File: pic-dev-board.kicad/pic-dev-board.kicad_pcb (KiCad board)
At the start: 2 copper layers, 100 x 100 mm, 74 parts, among them J1 Conn_GP0, J10 Jumper DATin, J11 Conn_SR_2, J12 Conn_SR_1, J13 Conn_5V_GND, J14 Jumper CLKin, J15 Barrel_Jack_Switch, J16 RUN/~PGM, J17 I2C, J18 GP1(RA1)/RB6, J19 GP2(RA2)/RB4, J2 Conn_GP4, J3 Conn_GP1, J4 Conn_GP5, J5 Conn_GP2, J6 Conn_ICSP, J7 Conn_TRISC, J8 Conn_TRISA, J9 Conn_TRISB, SW1 SW_Push, U1 PIC16F690-IP, U2 74HC595, U3 74HC595

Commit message: added second GP/TRISA connector
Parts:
- added J20: Conn_TRISA, Connector_PinHeader_2.54mm:PinHeader_1x07_P2.54mm_Vertical, F.Cu at (44.6, 104.0)
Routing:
- net /GP0: track 139.8 -> 222.0 mm
- net /GP1: track 114.7 -> 196.4 mm
- net /GP5: track 114.7 -> 196.4 mm
- net /GP4: track 112.4 -> 194.0 mm
- net /GP2: track 115.7 -> 197.4 mm
- net +5V: track 356.6 -> 389.5 mm
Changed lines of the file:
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@@
     (thickness 1.6)
     (drawings 8)
-    (tracks 648)
+    (tracks 672)
     (zones 0)
-    (modules 74)
+    (modules 75)
     (nets 88)
   )
@@
     (add_net /Vdd)
   )
+  (module Connector_PinHeader_2.54mm:PinHeader_1x07_P2.54mm_Vertical (layer F.Cu)
+    (at 44.6278 104.013)
+    (descr "Through hole straight pin header, 1x07, 2.54mm pitch, single row")
+    (tags "Through hole pin header THT 1x07 2.54mm single row")
+    (fp_text reference J20 (at 0 -2.33) (layer F.SilkS) hide
+      (effects (font (size 1 1) (thickness 0.15)))
+    )
+    (fp_text value Conn_TRISA (at 0 17.57) (layer F.Fab)
+      (effects (font (size 1 1) (thickness 0.15)))
+    )
+    (fp_text user %R (at 0 7.62 90) (layer F.Fab)
+      (effects (font (size 1 1) (thickness 0.15)))
+    )
+    (fp_line (start 1.8 -1.8) (end -1.8 -1.8) (layer F.CrtYd) (width 0.05))
+    (fp_line (start 1.8 17.05) (end 1.8 -1.8) (layer F.CrtYd) (width 0.05))
+    (fp_line (start -1.8 17.05) (end 1.8 17.05) (layer F.CrtYd) (width 0.05))
+    (fp_line (start -1.8 -1.8) (end -1.8 17.05) (layer F.CrtYd) (width 0.05))
+    (fp_line (start -1.33 -1.33) (end 0 -1.33) (layer F.SilkS) (width 0.12))
+    (fp_line (start -1.33 0) (end -1.33 -1.33) (layer F.SilkS) (width 0.12))
+    (fp_line (start -1.33 1.27) (end 1.33 1.27) (layer F.SilkS) (width 0.12))
+    (fp_line (start 1.33 1.27) (end 1.33 16.57) (layer F.SilkS) (width 0.12))
+    (fp_line (start -1.33 1.27) (end -1.33 16.57) (layer F.SilkS) (width 0.12))
+    (fp_line (start -1.33 16.57) (end 1.33 16.57) (layer F.SilkS) (width 0.12))
+    (fp_line (start -1.27 -0.635) (end -0.635 -1.27) (layer F.Fab) (width 0.1))
+    (fp_line (start -1.27 16.51) (end -1.27 -0.635) (layer F.Fab) (width 0.1))
+    (fp_line (start 1.27 16.51) (end -1.27 16.51) (layer F.Fab) (width 0.1))
+    (fp_line (start 1.27 -1.27) (end 1.27 16.51) (layer F.Fab) (width 0.1))
+    (fp_line (start -0.635 -1.27) (end 1.27 -1.27) (layer F.Fab) (width 0.1))
+    (pad 7 thru_hole oval (at 0 15.24) (size 1.7 1.7) (drill 1) (layers *.Cu *.Mask)
+      (net 53 +5V))
+    (pad 6 thru_hole oval (at 0 12.7) (size 1.7 1.7) (drill 1) (layers *.Cu *.Mask)
+      (net 2 GND))
+    (pad 5 thru_hole oval (at 0 10.16) (size 1.7 1.7) (drill 1) (layers *.Cu *.Mask)
+      (net 59 /GP5))
+    (pad 4 thru_hole oval (at 0 7.62) (size 1.7 1.7) (drill 1) (layers *.Cu *.Mask)
+      (net 55 /GP4))
+    (pad 3 thru_hole oval (at 0 5.08) (size 1.7 1.7) (drill 1) (layers *.Cu *.Mask)
+      (net 61 /GP2))
+    (pad 2 thru_hole oval (at 0 2.54) (size 1.7 1.7) (drill 1) (layers *.Cu *.Mask)
+      (net 57 /GP1))
+    (pad 1 thru_hole rect (at 0 0) (size 1.7 1.7) (drill 1) (layers *.Cu *.Mask)
+      (net 51 /GP0))
+    (model ${KISYS3DMOD}/Connector_PinHeader_2.54mm.3dshapes/PinHeader_1x07_P2.54mm_Vertical.wrl
+      (at (xyz 0 0 0))
+      (scale (xyz 1 1 1))
+      (rotate (xyz 0 0 0))
+    )
+  )
   (module user:PinHeader_2x15_P2.54mm_Vertical_Slim (layer F.Cu)
     (at 80.772 91.186)
@@
   (segment (start 122.174 89.962136) (end 122.174 101.938) (width 0.25) (layer F.Cu) (net 51))
   (segment (start 122.174 101.938) (end 124.122 103.886) (width 0.25) (layer F.Cu) (net 51))
+  (segment (start 44.6278 102.913) (end 44.6278 104.013) (width 0.25) (layer B.Cu) (net 51))
+  (segment (start 44.829801 102.710999) (end 44.6278 102.913) (width 0.25) (layer B.Cu) (net 51))
+  (segment (start 116.896001 102.710999) (end 44.829801 102.710999) (width 0.25) (layer B.Cu) (net 51))
+  (segment (start 118.071002 103.886) (end 116.896001 102.710999) (width 0.25) (layer B.Cu) (net 51))
+  (segment (start 125.222 103.886) (end 118.071002 103.886) (width 0.25) (layer B.Cu) (net 51))
   (segment (start 120.045389 31.602589) (end 53.055011 31.602589) (width 0.25) (layer F.Cu) (net 52))
   (segment (start 52.08 32.5776) (end 52.08 34.1276) (width 0.25) (layer F.Cu) (net 52))
@@
   (segment (start 47.4946 89.408) (end 71.12 89.408) (width 0.5) (layer F.Cu) (net 53))
   (segment (start 45.5896 87.503) (end 47.4946 89.408) (width 0.5) (layer F.Cu) (net 53))
-  (segment (start 43.7896 87.503) (end 45.5896 87.503) (width 0.5) (layer F.Cu) (net 53))
   (segment (start 43.7896 87.503) (end 43.7896 74.2442) (width 0.5) (layer B.Cu) (net 53))
   (segment (start 37.3126 67.7672) (end 33.274 67.7672) (width 0.5) (layer B.Cu) (net 53))
@@
   (segment (start 43.434 61.7991) (end 41.944098 61.7991) (width 0.5) (layer F.Cu) (net 53))
   (segment (start 43.434 61.7991) (end 46.4566 61.7991) (width 0.5) (layer F.Cu) (net 53))
+  (segment (start 46.451999 88.365399) (end 45.5896 87.503) (width 0.5) (layer F.Cu) (net 53))
+  (segment (start 46.451999 117.428801) (end 46.451999 88.365399) (width 0.5) (layer F.Cu) (net 53))
+  (segment (start 45.5896 87.503) (end 43.7896 87.503) (width 0.5) (layer F.Cu) (net 53))
+  (segment (start 44.6278 119.253) (end 46.451999 117.428801) (width 0.5) (layer F.Cu) (net 53))
   (segment (start 98.468 71.374) (end 96.4955 71.374) (width 0.25) (layer F.Cu) (net 54))
   (segment (start 99.568 71.374) (end 98.468 71.374) (width 0.25) (layer F.Cu) (net 54))
@@
   (segment (start 101.9048 82.804) (end 103.244399 84.143599) (width 0.25) (layer F.Cu) (net 55))
   (segment (start 104.807001 106.800003) (end 104.807001 88.957401) (width 0.25) (layer F.Cu) (net 55))
+  (segment (start 45.477799 110.783001) (end 44.6278 111.633) (width 0.25) (layer B.Cu) (net 55))
+  (segment (start 45.929801 110.330999) (end 45.477799 110.783001) (width 0.25) (layer B.Cu) (net 55))
+  (segment (start 124.046999 110.330999) (end 45.929801 110.330999) (width 0.25) (layer B.Cu) (net 55))
+  (segment (start 125.222 111.506) (end 124.046999 110.330999) (width 0.25) (layer B.Cu) (net 55))
   (segment (start 99.568 82.804) (end 96.4955 82.804) (width 0.25) (layer F.Cu) (net 56))
   (segment (start 50.546 48.514) (end 50.546 49.711002) (width 0.25) (layer F.Cu) (net 57))
@@
   (segment (start 115.64049 88.755488) (end 120.396 93.510998) (width 0.25) (layer F.Cu) (net 57))
   (segment (start 109.53249 83.113626) (end 109.53249 83.639354) (width 0.25) (layer F.Cu) (net 57))
+  (segment (start 45.477799 105.703001) (end 44.6278 106.553) (width 0.25) (layer B.Cu) (net 57))
+  (segment (start 46.119799 105.061001) (end 45.477799 105.703001) (width 0.25) (layer B.Cu) (net 57))
+  (segment (start 123.857001 105.061001) (end 46.119799 105.061001) (width 0.25) (layer B.Cu) (net 57))
+  (segment (start 125.222 106.426) (end 123.857001 105.061001) (width 0.25) (layer B.Cu) (net 57))
   (segment (start 98.468 75.184) (end 96.4955 75.184) (width 0.25) (layer F.Cu) (net 58))
   (segment (start 99.568 75.184) (end 98.468 75.184) (width 0.25) (layer F.Cu) (net 58))
@@
   (segment (start 100.584 85.2932) (end 101.8794 86.5886) (width 0.25) (layer F.Cu) (net 59))
   (segment (start 100.584 68.834) (end 100.584 85.2932) (width 0.25) (layer F.Cu) (net 59))
+  (segment (start 45.477799 115.022999) (end 44.6278 114.173) (width 0.25) (layer B.Cu) (net 59))
+  (segment (start 45.865799 115.410999) (end 45.477799 115.022999) (width 0.25) (layer B.Cu) (net 59))
+  (segment (start 123.857001 115.410999) (end 45.865799 115.410999) (width 0.25) (layer B.Cu) (net 59))
+  (segment (start 125.222 114.046) (end 123.857001 115.410999) (width 0.25) (layer B.Cu) (net 59))
   (segment (start 99.568 86.614) (end 96.4955 86.614) (width 0.25) (layer F.Cu) (net 60))
   (via (at 74.676 80.264) (size 0.8) (drill 0.4) (layers F.Cu B.Cu) (net 61))
@@
   (segment (start 115.156999 93.351997) (end 115.156999 94.290001) (width 0.25) (layer F.Cu) (net 61))
   (segment (start 116.896001 95.090999) (end 118.618 96.812998) (width 0.25) (layer F.Cu) (net 61))
+  (segment (start 45.477799 108.243001) (end 44.6278 109.093) (width 0.25) (layer B.Cu) (net 61))
+  (segment (start 124.046999 107.790999) (end 45.929801 107.790999) (width 0.25) (layer B.Cu) (net 61))
+  (segment (start 45.929801 107.790999) (end 45.477799 108.243001) (width 0.25) (layer B.Cu) (net 61))
+  (segment (start 125.222 108.966) (end 124.046999 107.790999) (width 0.25) (layer B.Cu) (net 61))
   (segment (start 99.568 78.994) (end 96.4955 78.994) (width 0.25) (layer F.Cu) (net 62))
   (segment (start 47.051 49.389) (end 47.051 48.514) (width 0.25) (layer F.Cu) (net 64))

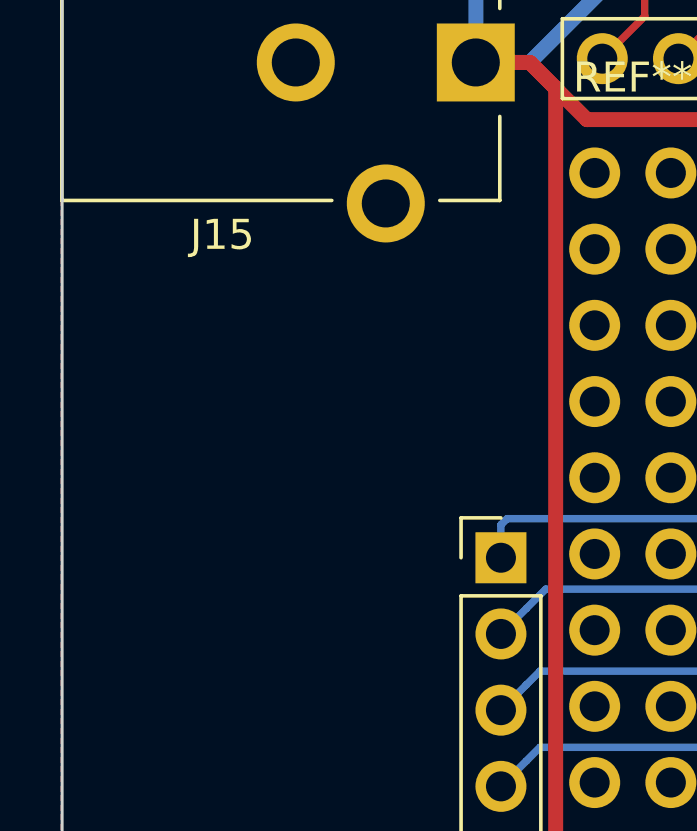
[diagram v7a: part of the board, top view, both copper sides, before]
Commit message: added footprint for SO-8
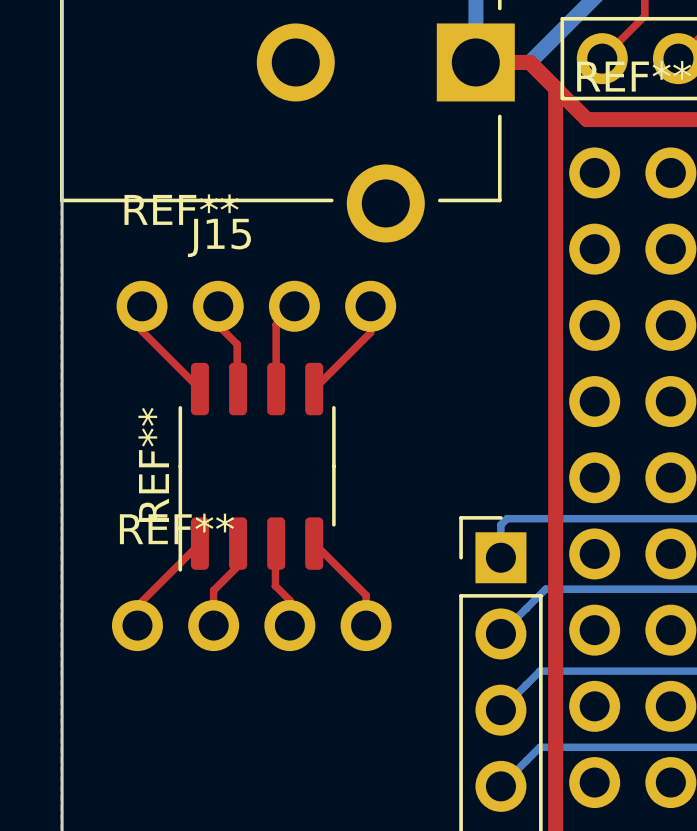
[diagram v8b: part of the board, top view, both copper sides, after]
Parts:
- added REF**: Proto_Area_04x01_P2.54mm_Drill1.0mm, Proto_Area:Proto_Area_04x01, F.Cu at (32.5, 106.3)
- added REF**: Proto_Area_04x01_P2.54mm_Drill1.0mm, Proto_Area:Proto_Area_04x01, F.Cu at (32.7, 95.6)
- added REF**: SO-8_3.9x4.9mm_P1.27mm, Package_SO:SO-8_3.9x4.9mm_P1.27mm, F.Cu at (36.5, 101.0)
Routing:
- net (no net): track 0.00 -> 26.2 mm
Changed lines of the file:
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@@
     (thickness 1.6)
     (drawings 8)
-    (tracks 672)
+    (tracks 693)
     (zones 0)
-    (modules 75)
+    (modules 78)
     (nets 88)
   )
@@
     (add_net /Vdd)
   )
+  (module Proto_Area:Proto_Area_04x01 (layer F.Cu)
+    (at 32.512 106.2736)
+    (descr "Prototyping Area")
+    (tags connector)
+    (attr virtual)
+    (fp_text reference REF** (at 1.27 -3.175) (layer F.SilkS)
+      (effects (font (size 1 1) (thickness 0.15)))
+    )
+    (fp_text value Proto_Area_04x01_P2.54mm_Drill1.0mm (at 1.27 5.08) (layer F.Fab)
+      (effects (font (size 1 1) (thickness 0.15)))
+    )
+    (fp_line (start 8.89 -1.27) (end 8.89 1.27) (layer F.CrtYd) (width 0.05))
+    (fp_line (start -1.27 1.27) (end 8.89 1.27) (layer F.CrtYd) (width 0.05))
+    (fp_line (start -1.27 -1.27) (end -1.27 1.27) (layer F.CrtYd) (width 0.05))
+    (fp_line (start -1.27 -1.27) (end 8.89 -1.27) (layer F.CrtYd) (width 0.05))
+    (fp_text user %R (at 1.27 1.27) (layer F.Fab)
+      (effects (font (size 1 1) (thickness 0.15)))
+    )
+    (pad 4 thru_hole circle (at 7.62 0) (size 1.7 1.7) (drill 1) (layers *.Cu *.Mask))
+    (pad 3 thru_hole circle (at 5.08 0) (size 1.7 1.7) (drill 1) (layers *.Cu *.Mask))
+    (pad 2 thru_hole circle (at 2.54 0) (size 1.7 1.7) (drill 1) (layers *.Cu *.Mask))
+    (pad 1 thru_hole circle (at 0 0) (size 1.7 1.7) (drill 1) (layers *.Cu *.Mask))
+  )
+  (module Proto_Area:Proto_Area_04x01 (layer F.Cu)
+    (at 32.6644 95.631)
+    (descr "Prototyping Area")
+    (tags connector)
+    (attr virtual)
+    (fp_text reference REF** (at 1.27 -3.175) (layer F.SilkS)
+      (effects (font (size 1 1) (thickness 0.15)))
+    )
+    (fp_text value Proto_Area_04x01_P2.54mm_Drill1.0mm (at 1.27 5.08) (layer F.Fab)
+      (effects (font (size 1 1) (thickness 0.15)))
+    )
+    (fp_line (start 8.89 -1.27) (end 8.89 1.27) (layer F.CrtYd) (width 0.05))
+    (fp_line (start -1.27 1.27) (end 8.89 1.27) (layer F.CrtYd) (width 0.05))
+    (fp_line (start -1.27 -1.27) (end -1.27 1.27) (layer F.CrtYd) (width 0.05))
+    (fp_line (start -1.27 -1.27) (end 8.89 -1.27) (layer F.CrtYd) (width 0.05))
+    (fp_text user %R (at 1.27 1.27) (layer F.Fab)
+      (effects (font (size 1 1) (thickness 0.15)))
+    )
+    (pad 4 thru_hole circle (at 7.62 0) (size 1.7 1.7) (drill 1) (layers *.Cu *.Mask))
+    (pad 3 thru_hole circle (at 5.08 0) (size 1.7 1.7) (drill 1) (layers *.Cu *.Mask))
+    (pad 2 thru_hole circle (at 2.54 0) (size 1.7 1.7) (drill 1) (layers *.Cu *.Mask))
+    (pad 1 thru_hole circle (at 0 0) (size 1.7 1.7) (drill 1) (layers *.Cu *.Mask))
+  )
+  (module Package_SO:SO-8_3.9x4.9mm_P1.27mm (layer F.Cu)
+    (at 36.4998 100.965 90)
+    (descr "SO, 8 Pin (https://www.nxp.com/docs/en/data-sheet/PCF8523.pdf), generated with kicad-footprint-generator ipc_gullwing_generator.py")
+    (tags "SO SO")
+    (attr smd)
+    (fp_text reference REF** (at 0 -3.4 90) (layer F.SilkS)
+      (effects (font (size 1 1) (thickness 0.15)))
+    )
+    (fp_text value SO-8_3.9x4.9mm_P1.27mm (at 0 3.4 90) (layer F.Fab)
+      (effects (font (size 1 1) (thickness 0.15)))
+    )
+    (fp_text user %R (at 0 0 90) (layer F.Fab)
+      (effects (font (size 0.98 0.98) (thickness 0.15)))
+    )
+    (fp_line (start 3.7 -2.7) (end -3.7 -2.7) (layer F.CrtYd) (width 0.05))
+    (fp_line (start 3.7 2.7) (end 3.7 -2.7) (layer F.CrtYd) (width 0.05))
+    (fp_line (start -3.7 2.7) (end 3.7 2.7) (layer F.CrtYd) (width 0.05))
+    (fp_line (start -3.7 -2.7) (end -3.7 2.7) (layer F.CrtYd) (width 0.05))
+    (fp_line (start -1.95 -1.475) (end -0.975 -2.45) (layer F.Fab) (width 0.1))
+    (fp_line (start -1.95 2.45) (end -1.95 -1.475) (layer F.Fab) (width 0.1))
+    (fp_line (start 1.95 2.45) (end -1.95 2.45) (layer F.Fab) (width 0.1))
+    (fp_line (start 1.95 -2.45) (end 1.95 2.45) (layer F.Fab) (width 0.1))
+    (fp_line (start -0.975 -2.45) (end 1.95 -2.45) (layer F.Fab) (width 0.1))
+    (fp_line (start 0 -2.56) (end -3.45 -2.56) (layer F.SilkS) (width 0.12))
+    (fp_line (start 0 -2.56) (end 1.95 -2.56) (layer F.SilkS) (width 0.12))
+    (fp_line (start 0 2.56) (end -1.95 2.56) (layer F.SilkS) (width 0.12))
+    (fp_line (start 0 2.56) (end 1.95 2.56) (layer F.SilkS) (width 0.12))
+    (pad 8 smd roundrect (at 2.575 -1.905 90) (size 1.75 0.6) (layers F.Cu F.Paste F.Mask) (roundrect_rratio 0.25))
+    (pad 7 smd roundrect (at 2.575 -0.635 90) (size 1.75 0.6) (layers F.Cu F.Paste F.Mask) (roundrect_rratio 0.25))
+    (pad 6 smd roundrect (at 2.575 0.635 90) (size 1.75 0.6) (layers F.Cu F.Paste F.Mask) (roundrect_rratio 0.25))
+    (pad 5 smd roundrect (at 2.575 1.905 90) (size 1.75 0.6) (layers F.Cu F.Paste F.Mask) (roundrect_rratio 0.25))
+    (pad 4 smd roundrect (at -2.575 1.905 90) (size 1.75 0.6) (layers F.Cu F.Paste F.Mask) (roundrect_rratio 0.25))
+    (pad 3 smd roundrect (at -2.575 0.635 90) (size 1.75 0.6) (layers F.Cu F.Paste F.Mask) (roundrect_rratio 0.25))
+    (pad 2 smd roundrect (at -2.575 -0.635 90) (size 1.75 0.6) (layers F.Cu F.Paste F.Mask) (roundrect_rratio 0.25))
+    (pad 1 smd roundrect (at -2.575 -1.905 90) (size 1.75 0.6) (layers F.Cu F.Paste F.Mask) (roundrect_rratio 0.25))
+    (model ${KISYS3DMOD}/Package_SO.3dshapes/SO-8_3.9x4.9mm_P1.27mm.wrl
+      (at (xyz 0 0 0))
+      (scale (xyz 1 1 1))
+      (rotate (xyz 0 0 0))
+    )
+  )
   (module Connector_PinHeader_2.54mm:PinHeader_1x07_P2.54mm_Vertical (layer F.Cu)
     (at 44.6278 104.013)
@@
   (gr_line (start 30 33) (end 30 127) (layer Edge.Cuts) (width 0.1))
   (gr_line (start 33 130) (end 127 130) (layer Edge.Cuts) (width 0.1))
+  (segment (start 32.6644 96.4596) (end 32.6644 95.631) (width 0.25) (layer F.Cu) (net 0))
+  (segment (start 34.5948 98.39) (end 32.6644 96.4596) (width 0.25) (layer F.Cu) (net 0))
+  (segment (start 40.2844 96.5104) (end 40.2844 95.631) (width 0.25) (layer F.Cu) (net 0))
+  (segment (start 38.4048 98.39) (end 40.2844 96.5104) (width 0.25) (layer F.Cu) (net 0))
+  (segment (start 40.132 105.2672) (end 40.132 106.2736) (width 0.25) (layer F.Cu) (net 0))
+  (segment (start 38.4048 103.54) (end 40.132 105.2672) (width 0.25) (layer F.Cu) (net 0))
+  (segment (start 32.512 105.6228) (end 32.512 106.2736) (width 0.25) (layer F.Cu) (net 0))
+  (segment (start 34.5948 103.54) (end 32.512 105.6228) (width 0.25) (layer F.Cu) (net 0))
+  (segment (start 35.052 106.2736) (end 35.052 105.1052) (width 0.25) (layer F.Cu) (net 0))
+  (segment (start 35.8648 104.2924) (end 35.8648 103.54) (width 0.25) (layer F.Cu) (net 0))
+  (segment (start 35.052 105.1052) (end 35.8648 104.2924) (width 0.25) (layer F.Cu) (net 0))
+  (segment (start 37.592 105.4354) (end 37.592 106.2736) (width 0.25) (layer F.Cu) (net 0))
+  (segment (start 37.1094 104.9528) (end 37.592 105.4354) (width 0.25) (layer F.Cu) (net 0))
+  (segment (start 37.1348 103.54) (end 37.1094 103.5654) (width 0.25) (layer F.Cu) (net 0))
+  (segment (start 37.1094 103.5654) (end 37.1094 104.9528) (width 0.25) (layer F.Cu) (net 0))
+  (segment (start 35.8394 98.3646) (end 35.8648 98.39) (width 0.25) (layer F.Cu) (net 0))
+  (segment (start 35.2044 95.631) (end 35.2044 96.266) (width 0.25) (layer F.Cu) (net 0))
+  (segment (start 35.8394 96.901) (end 35.8394 98.3646) (width 0.25) (layer F.Cu) (net 0))
+  (segment (start 35.2044 96.266) (end 35.8394 96.901) (width 0.25) (layer F.Cu) (net 0))
+  (segment (start 37.1348 96.2406) (end 37.1348 98.39) (width 0.25) (layer F.Cu) (net 0))
+  (segment (start 37.7444 95.631) (end 37.1348 96.2406) (width 0.25) (layer F.Cu) (net 0))
   (segment (start 55.5 53) (end 54 51.5) (width 0.5) (layer F.Cu) (net 1))
   (segment (start 58 53) (end 55.5 53) (width 0.5) (layer F.Cu) (net 1))
